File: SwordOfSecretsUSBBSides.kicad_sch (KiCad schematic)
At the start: 34 parts, among them J1 DebugEdge_02x05, J2 USB_A, J5 Conn_01x03_Pin, SW1 SW_Push, SW3 SW_Push, U2 AMS1117-3.3, U3 W25Q128JVS, U4 CH32V003F4P6, U5 CH340E

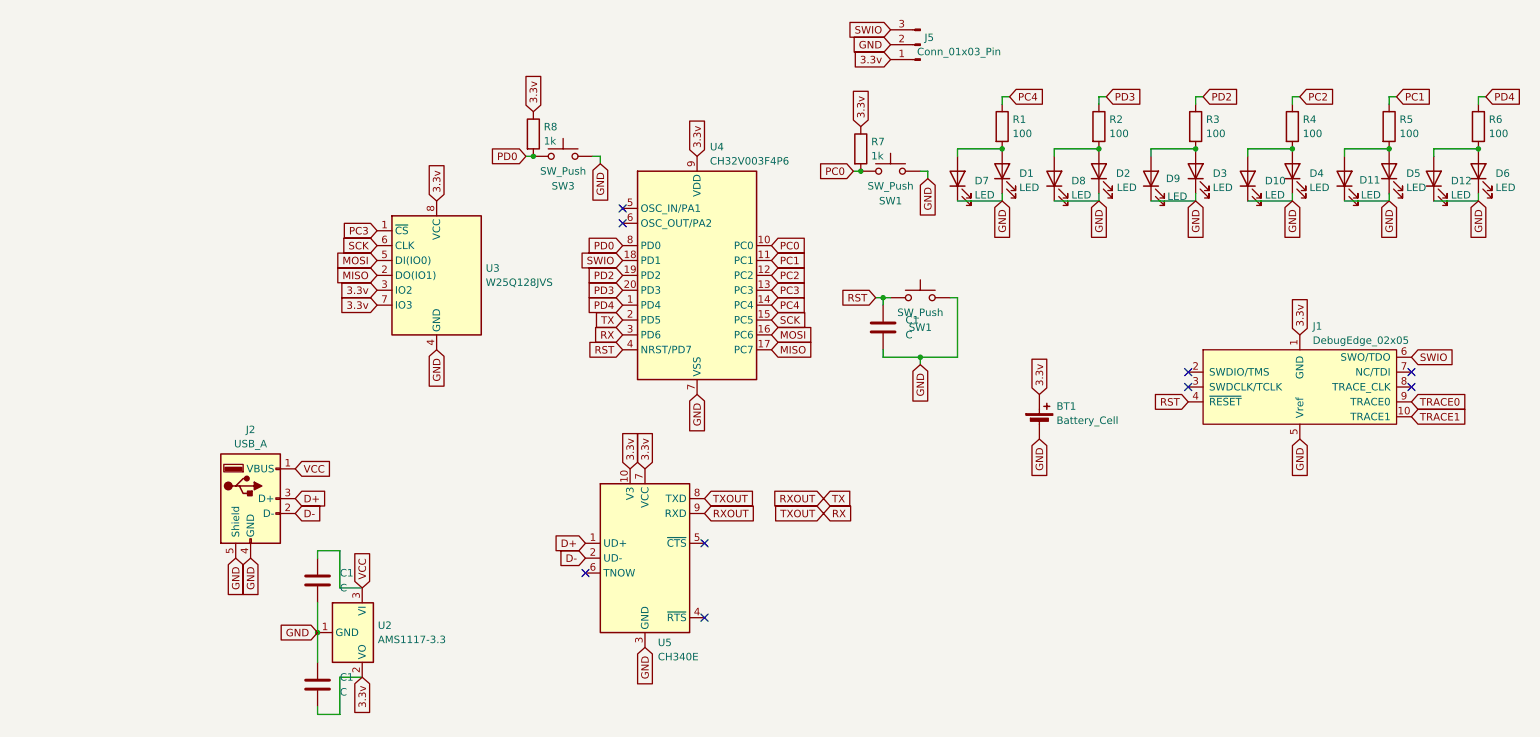
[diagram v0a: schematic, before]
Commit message: Fixing debug edge to include UART, adding protection diodes to 3.3v lines from battery and LDO and adding boost converter to ensure 3.3v from battery
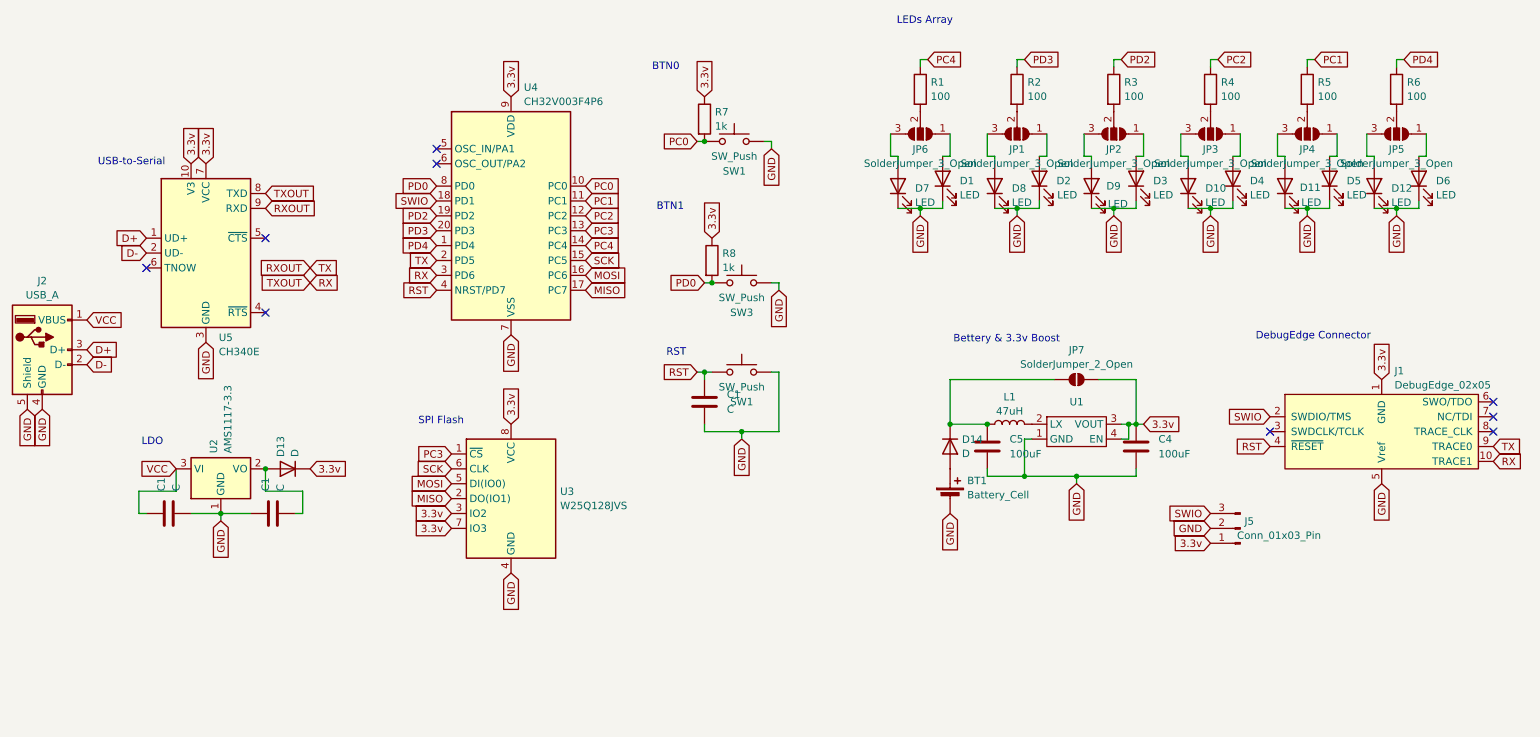
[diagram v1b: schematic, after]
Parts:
- added C4, C5: 100uF, Capacitor_SMD:C_0805_2012Metric_Pad1.18x1.45mm_HandSolder, symbol Device:C
- added D13, D14: D, Diode_SMD:D_SOD-123, symbol Device:D
- added JP1, JP2, JP3, JP4, JP5, JP6: SolderJumper_3_Open, SolderJumper:SolderJumper-3_P1.3mm_Open_RoundedPad1.0x1.5mm_NumberLabels, symbol Jumper:SolderJumper_3_Open
- added JP7: SolderJumper_2_Open, SolderJumper:SolderJumper-2_P1.3mm_Open_RoundedPad1.0x1.5mm, symbol Jumper:SolderJumper_2_Open
- added L1: 47uH, Inductor_SMD:L_Ferrocore_DLG-0403, symbol Device:L
- added U1: ~, QX2304L33T:QX2304L33T, symbol QX2304LXXX:QX2304LXXX
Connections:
- net TRACE0 is gone; now on net RXOUT: J1.9 (TRACE0)
- net TRACE1 is gone; now on net RX: J1.10 (TRACE1)
- net 3.3v: now also C4.1, D13.1 (K), JP7.2 (B), U1.3 (VOUT), U1.4 (EN); no longer BT1.1 (+), C1.2, U2.2 (VO)
- net GND: now also C4.2, C5.2, U1.1 (GND)
- net SWIO: now also J1.2 (SWDIO/TMS); no longer J1.6 (SWO/TDO)
- new net: D4.2 (A), JP3.1 (A)
- new net: JP3.2 (C), R4.2
- new net: D10.2 (A), JP3.3 (B)
- new net: D11.2 (A), JP4.3 (B)
- new net: C5.1, D14.1 (K), JP7.1 (A), L1.1
- new net: BT1.1 (+), D14.2 (A)
- new net: C1.2, D13.2 (A), U2.2 (VO)
- new net: JP1.2 (C), R2.2
- new net: D2.2 (A), JP1.1 (A)
- new net: D9.2 (A), JP2.3 (B)
- new net: D5.2 (A), JP4.1 (A)
- new net: D1.2 (A), JP6.1 (A)
- new net: JP6.2 (C), R1.2
- new net: D7.2 (A), JP6.3 (B)
- new net: L1.2, U1.2 (LX)
- new net: D3.2 (A), JP2.1 (A)
- new net: D8.2 (A), JP1.3 (B)
- new net: JP5.2 (C), R6.2
- new net: JP2.2 (C), R3.2
- new net: D6.2 (A), JP5.1 (A)
- new net: D12.2 (A), JP5.3 (B)
- new net: JP4.2 (C), R5.2
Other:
- note added: "BTN0"
- note added: "BTN1"
- note added: "Bettery & 3.3v Boost"
- note added: "DebugEdge Connector"
- note added: "LDO"
- note added: "LEDs Array"
- note added: "RST"
- note added: "SPI Flash"
- note added: "USB-to-Serial"
- moved on the sheet: BT1, C1, D1, D10, D11, D12, D2, D3, D4, D5, D6, D7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

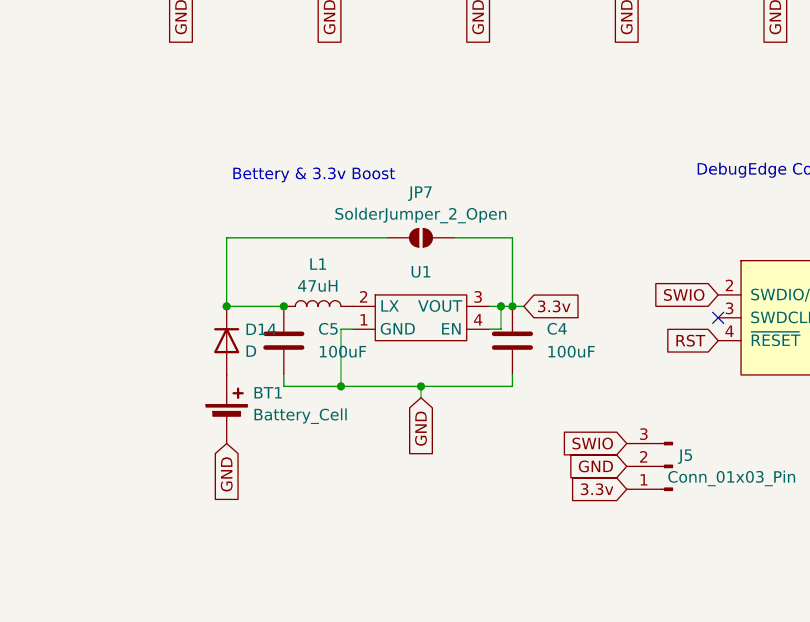
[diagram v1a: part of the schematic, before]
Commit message: Changed battery, fixed side-mouted LED orientation
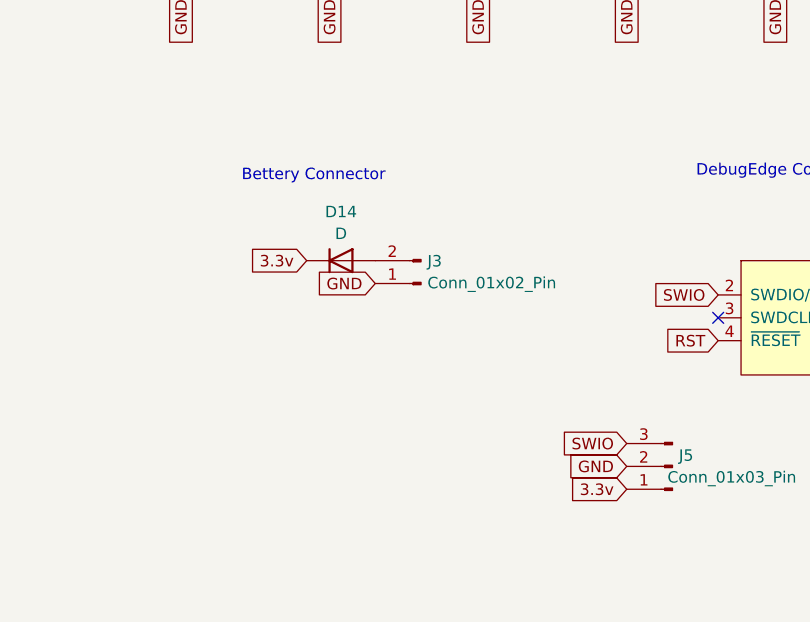
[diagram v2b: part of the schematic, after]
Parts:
- removed BT1: Battery_Cell, Battery:MY-1025-01, symbol Device:Battery_Cell
- removed C4, C5: 100uF, Capacitor_SMD:C_0805_2012Metric_Pad1.18x1.45mm_HandSolder, symbol Device:C
- removed JP7: SolderJumper_2_Open, SolderJumper:SolderJumper-2_P1.3mm_Open_RoundedPad1.0x1.5mm, symbol Jumper:SolderJumper_2_Open
- removed L1: 47uH, Inductor_SMD:L_Ferrocore_DLG-0403, symbol Device:L
- removed U1: ~, QX2304L33T:QX2304L33T, symbol QX2304LXXX:QX2304LXXX
- added J3: Conn_01x02_Pin, Connector_PinHeader_2.54mm:PinHeader_1x02_P2.54mm_Vertical, symbol Connector:Conn_01x02_Pin
- C1: footprint Capacitor_SMD:C_0805_2012Metric_Pad1.18x1.45mm_HandSolder -> Capacitor_SMD:C_1206_3216Metric_Pad1.33x1.80mm_HandSolder
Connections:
- net 3.3v: now also D14.1 (K)
- net GND: now also J3.1 (Pin_1)
- net at D14.2 (A): now also J3.2 (Pin_2)
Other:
- note added: "Bettery Connector"
- note removed: "Bettery & 3.3v Boost"
- moved on the sheet: D14

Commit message: Production fixes
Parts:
- added BT1, BT2: BATTERY-AAA, Battery:BH-AAA-A1AJ001, symbol SparkFun-Batteries:BATTERY-AAA
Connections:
- net 3.3v: now also BT1.PWR@ (+)
- net GND: now also BT2.GND@ (-)
- new net: BT1.GND@ (-), BT2.PWR@ (+)
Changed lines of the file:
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@@
 	(wire
 		(pts
+			(xy 185.42 134.62) (xy 186.69 134.62)
+		)
+		(stroke
+			(width 0)
+			(type default)
+		)
+	)
+	(wire
+		(pts
 			(xy 44.45 132.08) (xy 45.72 132.08)
 		)
@@
 	(wire
 		(pts
+			(xy 163.83 134.62) (xy 165.1 134.62)
+		)
+		(stroke
+			(width 0)
+			(type default)
+		)
+	)
+	(wire
+		(pts
 			(xy 140.97 116.84) (xy 140.97 118.11)
 		)
@@
 	(global_label "GND"
 		(shape input)
+		(at 186.69 134.62 0)
+		(fields_autoplaced yes)
+		(effects
+			(font
+				(size 1.27 1.27)
+			)
+			(justify left)
+		)
+		(property "Intersheetrefs" "${INTERSHEET_REFS}"
+			(at 193.5457 134.62 0)
+			(effects
+				(font
+					(size 1.27 1.27)
+				)
+				(justify left)
+				(hide yes)
+			)
+		)
+	)
+	(global_label "GND"
+		(shape input)
 		(at 227.33 81.28 270)
 		(fields_autoplaced yes)
@@
 	(global_label "3.3v"
 		(shape input)
+		(at 163.83 134.62 180)
+		(fields_autoplaced yes)
+		(effects
+			(font
+				(size 1.27 1.27)
+			)
+			(justify right)
+		)
+		(property "Intersheetrefs" "${INTERSHEET_REFS}"
+			(at 156.8534 134.62 0)
+			(effects
+				(font
+					(size 1.27 1.27)
+				)
+				(justify right)
+				(hide yes)
+			)
+		)
+	)
+	(global_label "3.3v"
+		(shape input)
 		(at 107.95 116.84 90)
 		(fields_autoplaced yes)
@@
 	)
 	(symbol
+		(lib_name "SparkFun-Batteries:BATTERY-AAA")
+		(lib_id "SparkFun-Batteries:BATTERY-AAA")
+		(at 170.18 134.62 0)
+		(unit 1)
+		(exclude_from_sim no)
+		(in_bom yes)
+		(on_board yes)
+		(dnp no)
+		(fields_autoplaced yes)
+		(property "Reference" "BT1"
+			(at 170.18 127.099 0)
+			(effects
+				(font
+					(size 1.143 1.143)
+				)
+			)
+		)
+		(property "Value" "BATTERY-AAA"
+			(at 170.18 129.319 0)
+			(effects
+				(font
+					(size 1.143 1.143)
+				)
+			)
+		)
+		(property "Footprint" "Battery:BH-AAA-A1AJ001"
+			(at 170.18 128.27 0)
+			(effects
+				(font
+					(size 0.508 0.508)
+				)
+				(hide yes)
+			)
+		)
+		(property "Datasheet" ""
+			(at 170.18 134.62 0)
+			(effects
+				(font
+					(size 1.27 1.27)
+				)
+				(hide yes)
+			)
+		)
+		(property "Description" "Battery - Single Cell A variety of battery chemistries, sizes, and footprints. Device List:<ul><li><b>20MM_PTH - </b> <a href=\"https://www.sparkfun.com/products/783\">Coin Cell Battery Holder - 20mm (PTH)</a></li><li><b>6.8MM_PTH - </b> <a href=\"https://www.digikey.com/product-detail/en/seiko-instruments/MS621FE-FL11E/728-1057-ND/1889208?WT.srch=1&gclid=CNOQ5a6LzdQCFZS2wAodXCkE0g\">Coin Cell Battery Holder - 6.8MM(SMD)</a></li><li><b>12MM_SMD - </b> <a href=\"https://www.sparkfun.com/products/10592\">Coin Cell Battery Holder - 12mm (SMD)</a></li><li><b>12MM_PTH - </b><a href=\"https://www.sparkfun.com/products/7948\">Coin Cell Battery Holder - 12mm (PTH)</a></li><li><b>20MM_SMD - </b> 20mm Coin Cell Battery Holder (SMD) (2 legs)</li><ul><li>Used on the <a href=\"https://www.sparkfun.com/products/11734\">Big Time Watch Kit</a></li></ul><li><b>20MM_SMD_4LEGS - </b> <a href=\"https://www.sparkfun.com/products/11892\">Coin Cell Battery Holder - 20mm (SMD)</a></li><li><b>20MM_SMD_4LEGS_OVERPASTE - </b> <a href=\"https://www.sparkfun.com/products/11892\">Coin Cell Battery Holder - 20mm (SMD)</a> (Over-paste on the legs)</li><li><b>24.5MM_PTH - </b> <a href=\"https://www.sparkfun.com/products/8863\">Coin Cell Battery Holder - 24.5mm (PTH)</a></li><li><b>9V - </b> 9V Battery Holder - PC Mount </li><ul><li>Used on the <a href=\"https://www.sparkfun.com/products/11177\">SparkFun SparkPunk Sound Kit </a> and <a href=\"https://www.sparkfun.com/products/12707\">SparkFun SparkPunk Sequencer Kit </a></li></ul><li><b>18650 - </b> <a href=\"https://www.sparkfun.com/products/13113\">Battery Holder - 18650 (PTH)</a></li><li><b>AA - </b> <a href=\"https://www.sparkfun.com/products/7949\">Battery Holder - 1xAA (PTH)</a></li><li><b>AAA - </b> <a href=\"https://www.sparkfun.com/products/12718\">Battery Holder - 1xAAA (PTH)</a></li><li><b>AA_KIT - </b> <a href=\"https://www.sparkfun.com/products/7949\">Battery Holder - 1xAA (PTH)</a></li><ul><li>Special kit package - pads only have exposed copper on one side of the board.</li></ul><li><b>AAA_KIT - </b> <a href=\"https://www.sparkfun.com/products/12718\">Battery Holder - 1xAAA (PTH)</a></li><ul><li>Special kit package - pads only have exposed copper on one side of the board.</li></ul></ul>"
+			(at 170.18 134.62 0)
+			(effects
+				(font
+					(size 1.27 1.27)
+				)
+				(hide yes)
+			)
+		)
+		(property "" ""
+			(at 170.18 134.62 0)
+			(effects
+				(font
+					(size 1.524 1.524)
+				)
+				(hide yes)
+			)
+		)
+		(pin "PWR@"
+		)
+		(pin "GND@"
+		)
+		(instances
+			(project ""
+				(path "/7b0e6896-478b-4ede-9ff6-b6a5f526bf1e"
+					(reference "BT1")
+					(unit 1)
+				)
+			)
+		)
+	)
+	(symbol
 		(lib_id "Device:LED")
 		(at 207.01 76.2 90)
@@
 					(unit 1)
 				)
+			)
+		)
+	)
+	(symbol
+		(lib_name "SparkFun-Batteries:BATTERY-AAA")
+		(lib_id "SparkFun-Batteries:BATTERY-AAA")
+		(at 180.34 134.62 0)
+		(unit 1)
+		(exclude_from_sim no)
+		(in_bom yes)
+		(on_board yes)
+		(dnp no)
+		(fields_autoplaced yes)
+		(property "Reference" "BT2"
+			(at 180.34 127.099 0)
+			(effects
+				(font
+					(size 1.143 1.143)
+				)
+			)
+		)
+		(property "Value" "BATTERY-AAA"
+			(at 180.34 129.319 0)
+			(effects
+				(font
+					(size 1.143 1.143)
+				)
+			)
+		)
+		(property "Footprint" "Battery:BH-AAA-A1AJ001"
+			(at 180.34 128.27 0)
+			(effects
+				(font
+					(size 0.508 0.508)
+				)
+				(hide yes)
+			)
+		)
+		(property "Datasheet" ""
+			(at 180.34 134.62 0)
+			(effects
+				(font
+					(size 1.27 1.27)
+				)
+				(hide yes)
+			)
+		)
+		(property "Description" "Battery - Single Cell A variety of battery chemistries, sizes, and footprints. Device List:<ul><li><b>20MM_PTH - </b> <a href=\"https://www.sparkfun.com/products/783\">Coin Cell Battery Holder - 20mm (PTH)</a></li><li><b>6.8MM_PTH - </b> <a href=\"https://www.digikey.com/product-detail/en/seiko-instruments/MS621FE-FL11E/728-1057-ND/1889208?WT.srch=1&gclid=CNOQ5a6LzdQCFZS2wAodXCkE0g\">Coin Cell Battery Holder - 6.8MM(SMD)</a></li><li><b>12MM_SMD - </b> <a href=\"https://www.sparkfun.com/products/10592\">Coin Cell Battery Holder - 12mm (SMD)</a></li><li><b>12MM_PTH - </b><a href=\"https://www.sparkfun.com/products/7948\">Coin Cell Battery Holder - 12mm (PTH)</a></li><li><b>20MM_SMD - </b> 20mm Coin Cell Battery Holder (SMD) (2 legs)</li><ul><li>Used on the <a href=\"https://www.sparkfun.com/products/11734\">Big Time Watch Kit</a></li></ul><li><b>20MM_SMD_4LEGS - </b> <a href=\"https://www.sparkfun.com/products/11892\">Coin Cell Battery Holder - 20mm (SMD)</a></li><li><b>20MM_SMD_4LEGS_OVERPASTE - </b> <a href=\"https://www.sparkfun.com/products/11892\">Coin Cell Battery Holder - 20mm (SMD)</a> (Over-paste on the legs)</li><li><b>24.5MM_PTH - </b> <a href=\"https://www.sparkfun.com/products/8863\">Coin Cell Battery Holder - 24.5mm (PTH)</a></li><li><b>9V - </b> 9V Battery Holder - PC Mount </li><ul><li>Used on the <a href=\"https://www.sparkfun.com/products/11177\">SparkFun SparkPunk Sound Kit </a> and <a href=\"https://www.sparkfun.com/products/12707\">SparkFun SparkPunk Sequencer Kit </a></li></ul><li><b>18650 - </b> <a href=\"https://www.sparkfun.com/products/13113\">Battery Holder - 18650 (PTH)</a></li><li><b>AA - </b> <a href=\"https://www.sparkfun.com/products/7949\">Battery Holder - 1xAA (PTH)</a></li><li><b>AAA - </b> <a href=\"https://www.sparkfun.com/products/12718\">Battery Holder - 1xAAA (PTH)</a></li><li><b>AA_KIT - </b> <a href=\"https://www.sparkfun.com/products/7949\">Battery Holder - 1xAA (PTH)</a></li><ul><li>Special kit package - pads only have exposed copper on one side of the board.</li></ul><li><b>AAA_KIT - </b> <a href=\"https://www.sparkfun.com/products/12718\">Battery Holder - 1xAAA (PTH)</a></li><ul><li>Special kit package - pads only have exposed copper on one side of the board.</li></ul></ul>"
+			(at 180.34 134.62 0)
+			(effects
+				(font
+					(size 1.27 1.27)
+				)
+				(hide yes)
+			)
+		)
+		(property "" ""
+			(at 180.34 134.62 0)
+			(effects
+				(font
+					(size 1.524 1.524)
+				)
+				(hide yes)
+			)
+		)
+		(pin "PWR@"
+		)
+		(pin "GND@"
+		)
+		(instances
+			(project ""
+				(path "/7b0e6896-478b-4ede-9ff6-b6a5f526bf1e"
+					(reference "BT2")
+					(unit 1)
+				)

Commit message: Fixing schematics
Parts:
- BT1, BT2: 0 (none) -> 0
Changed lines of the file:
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@@
 			)
 		)
-		(property "" ""
+		(property "0" "0"
 			(at 170.18 134.62 0)
 			(effects
@@
 			)
 		)
-		(property "" ""
+		(property "0" "0"
 			(at 180.34 134.62 0)
 			(effects

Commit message: Fixing according to comments
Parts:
- removed J1: DebugEdge_02x05, DebugEdge_2x05_Target:DebugEdge_2x05_Target, symbol debugedge_02x05:DebugEdge_02x05
- C1: value C -> 100uF
- C1: value C -> 100nF
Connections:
- net GND: no longer J2.5 (Shield)
- no-connect marks 9 -> 5
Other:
- note added: "Bettery"
- note removed: "Bettery Connector"
- note removed: "DebugEdge Connector"

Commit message: WIP Production-ready files
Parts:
- removed D10, D11, D12, D7, D8, D9: LED, LED_SMD:LED_1206_3216Metric_ReverseMount_Hole1.8x2.4mm, symbol Device:LED
- removed JP1, JP2, JP3, JP4, JP5, JP6: SolderJumper_3_Open, SolderJumper:SolderJumper-3_P1.3mm_Open_RoundedPad1.0x1.5mm_NumberLabels, symbol Jumper:SolderJumper_3_Open
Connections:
- net at D4.2 (A): now also R4.2
- net at R2.2: now also D2.2 (A)
- net at D5.2 (A): now also R5.2
- net at D1.2 (A): now also R1.2
- net at D3.2 (A): now also R3.2
- net at R6.2: now also D6.2 (A)
